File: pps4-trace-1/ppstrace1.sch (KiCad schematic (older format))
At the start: 15 parts, among them J1 Conn_01x08_Male, J2 Conn_01x12_Male, J3 Conn_01x02_Male, U1 LM7805_TO220, U2 BP

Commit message: Added files
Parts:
- removed C1: C_Small, Capacitor_SMD:C_0805_2012Metric_Pad1.15x1.40mm_HandSolder, symbol Device:C_Small
- removed D2, D3: 1N4148, Diode_SMD:D_SOD-123, symbol Diode:1N4148
- added A1: SD_Card_Module_catalex, Charleslabs_Parts:SD_Card_Module, symbol Charleslabs_Parts:SD_Card_Module_catalex
- added J4, J7, J8, J9: Conn_01x04_Male, Connector_PinHeader_2.54mm:PinHeader_1x04_P2.54mm_Vertical, symbol Connector:Conn_01x04_Male
- added J5: Conn_01x03_Male, Connector_PinHeader_2.54mm:PinHeader_1x03_P2.54mm_Vertical, symbol Connector:Conn_01x03_Male
- added J6: Conn_01x05_Male, Connector_PinHeader_2.54mm:PinHeader_1x05_P2.54mm_Vertical, symbol Connector:Conn_01x05_Male
- added R10, R3, R4, R5, R6, R7, R8, R9: 10R, Resistor_THT:R_Axial_DIN0207_L6.3mm_D2.5mm_P10.16mm_Horizontal, symbol Device:R_Small
- D1: footprint (none) -> Diode_THT:D_5KPW_P12.70mm_Horizontal
- J1: renamed from J3; footprint (none) -> Connector_PinHeader_2.54mm:PinHeader_1x02_P2.54mm_Vertical
- J2: renamed from J1; footprint (none) -> Connector_PinHeader_2.54mm:PinHeader_1x08_P2.54mm_Vertical
- J3: renamed from J2; footprint (none) -> Connector_PinHeader_2.54mm:PinHeader_1x12_P2.54mm_Vertical
- R1, R2: value R_Small -> 10R; footprint (none) -> Resistor_THT:R_Axial_DIN0207_L6.3mm_D2.5mm_P10.16mm_Horizontal
- R11: renamed from R3; footprint (none) -> Resistor_THT:R_Axial_DIN0207_L6.3mm_D2.5mm_P10.16mm_Horizontal
- renumbered C2 to C1, C3 to C2, C4 to C3, U2 to U1, U1 to U2
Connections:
- net +3V3: now also U1.3V3 (3.3V), A1.2 (3V3)
- net GND: now also A1.1 (GND); no longer R2.2
- net ID1: now reaches U1.PA0
- net ID2: now reaches U1.PA1
- net ID7: now reaches U1.PA10
- net ID8: now reaches U1.PA11
- net ICLKB: now reaches U1.PA12
- net ICLKA: now reaches U1.PA15
- net ID3: now reaches U1.PA2
- net ID4: now reaches U1.PA3
- net at U1.PA4: now also J9.1 (Pin_1)
- net at U1.PA5: now also J9.2 (Pin_2)
- net at U1.PA6: now also J9.3 (Pin_3)
- net at U1.PA7: now also J9.4 (Pin_4)
- net ID5: now reaches U1.PA8
- net ID6: now reaches U1.PA9
- net IDO1: now reaches U1.PB0
- net IX5: now reaches U1.PB1
- net IA7: now reaches U1.PB10
- net IA8: now reaches U1.PB11
- net IA9: now reaches U1.PB12
- net IA10: now reaches U1.PB13
- net IA11: now reaches U1.PB14
- net IA12: now reaches U1.PB15
- net IWIO: now reaches U1.PB3
- net IA1: now reaches U1.PB4
- net IA2: now reaches U1.PB5
- net IA3: now reaches U1.PB6
- net IA4: now reaches U1.PB7
- net IA5: now reaches U1.PB8
- net IA6: now reaches U1.PB9
- net IDO3: now reaches U1.PC14
- net IDO4: now reaches U1.PC15
- net at R1.1: now also R2.2; no longer J2.1 (Pin_1)
- net D2: now reaches J2.2 (Pin_2)
- net D3: now reaches J2.3 (Pin_3)
- net D4: now reaches J2.4 (Pin_4)
- net D5: now reaches J2.5 (Pin_5)
- net D6: now reaches J2.6 (Pin_6)
- net D7: now reaches J2.7 (Pin_7)
- net D8: now reaches J2.8 (Pin_8)
- net A1: now reaches J3.1 (Pin_1)
- net A10: now reaches J3.10 (Pin_10)
- net A11: now reaches J3.11 (Pin_11)
- net A12: now reaches J3.12 (Pin_12)
- net A2: now reaches J3.2 (Pin_2)
- net A3: now reaches J3.3 (Pin_3)
- net A4: now reaches J3.4 (Pin_4)
- net A5: now reaches J3.5 (Pin_5)
- net A6: now reaches J3.6 (Pin_6)
- net A7: now reaches J3.7 (Pin_7)
- net A8: now reaches J3.8 (Pin_8)
- net A9: now reaches J3.9 (Pin_9)
- net at J1.1 (Pin_1): now also R1.2; no longer R11.2
- new net: R10.1, R11.2
- new net: R2.1, R3.2
- new net: R3.1, R4.2
- new net: R4.1, R5.2
- new net: R5.1, R6.2
- new net: R6.1, R7.2
- new net: R7.1, R8.2
- new net: R8.1, R9.2
- new net: R10.2, R9.1
- new net: A1.3 (MISO), J8.4 (Pin_4)
- new net: A1.4 (MOSI), J8.2 (Pin_2)
- new net: A1.5 (CLK), J8.3 (Pin_3)
- new net: A1.6 (CS), J8.1 (Pin_1)
- new net CLKA: J5.1 (Pin_1)
- new net CLKB: J5.2 (Pin_2)
- new net D1: J2.1 (Pin_1)
- new net DO1: J4.1 (Pin_1)
- new net DO2: J4.2 (Pin_2)
- new net DO3: J4.3 (Pin_3)
- new net DO4: J4.4 (Pin_4)
- new net IDO2: U1.PC13
- new net IX1: J7.1 (Pin_1)
- new net IX2: J7.2 (Pin_2)
- new net IX3: J7.3 (Pin_3)
- new net IX4: J7.4 (Pin_4)
- new net WIO: J5.3 (Pin_3)
- new net X1: J6.1 (Pin_1)
- new net X2: J6.2 (Pin_2)
- new net X3: J6.3 (Pin_3)
- new net X4: J6.4 (Pin_4)
- new net X5: J6.5 (Pin_5)
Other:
- moved on the sheet: C1, C2, C3, D1, J1, R11, U2

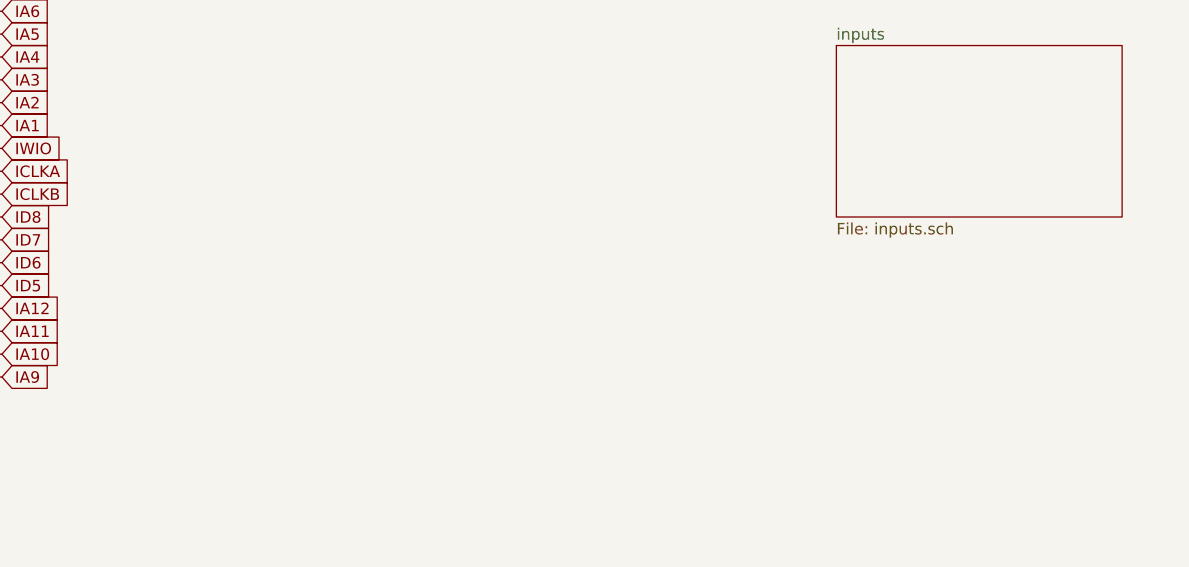
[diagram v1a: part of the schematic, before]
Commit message: Added more traces, some broken. Trace processing script now decodes successfully after fixes to input processing.
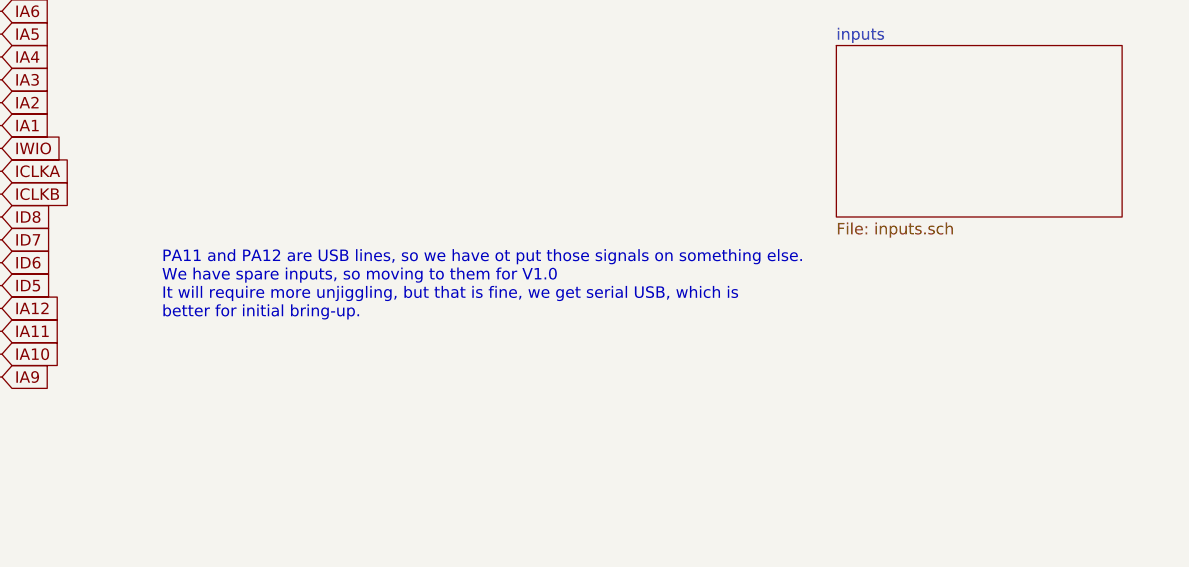
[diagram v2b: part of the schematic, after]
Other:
- note added: "PA11 and PA12 are USB lines, so we have ot put those signals on something else.\nWe have spare inputs, so moving to them for V1.0\nIt will require more unjiggling, but that is fine, we get serial USB, which is\nbetter for initial bring-up.\n"
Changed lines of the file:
@@
 	1    0    0    -1
 $EndComp
+Text Notes 6250 2750 0    50   ~ 0
+PA11 and PA12 are USB lines, so we have ot put those signals on something else.\nWe have spare inputs, so moving to them for V1.0\nIt will require more unjiggling, but that is fine, we get serial USB, which is\nbetter for initial bring-up.\n
 $EndSCHEMATC
